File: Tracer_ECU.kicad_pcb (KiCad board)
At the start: 4 copper layers, 80 x 55 mm, 166 parts, among them IC1 R5F572TFADFP#30, IC2 MPU-6500, IC3 DRV8320HRTVR, IC4 DRV8320HRTVR, IC5 DRV8320HRTVR, J1 BAT, J10 ENC2, J11 SENS2, J13 SDC, J14 ENC3, J2 DBG, J3 SENS1, J4 MOT3, J5 MOT1, J6 LIGHIT, J8 MOT2, J9 ENC1, Q1 TJ60S04M3L, Q10 FDS6898A, Q11 FDS6898A, Q12 FDS6898A, Q2 FDS6898A, Q3 FDS6898A, Q4 FDS6898A, Q6 IRLML6344TRPBF, Q7 FDS6898A, Q8 FDS6898A, Q9 FDS6898A, SW1 SW_SPDT, SW2 SW_Push, SW4 SW_Push, SW5 SW_Push, U1 NJM2732, U2 AZ1117-3.3, Y1 CSTNE20M

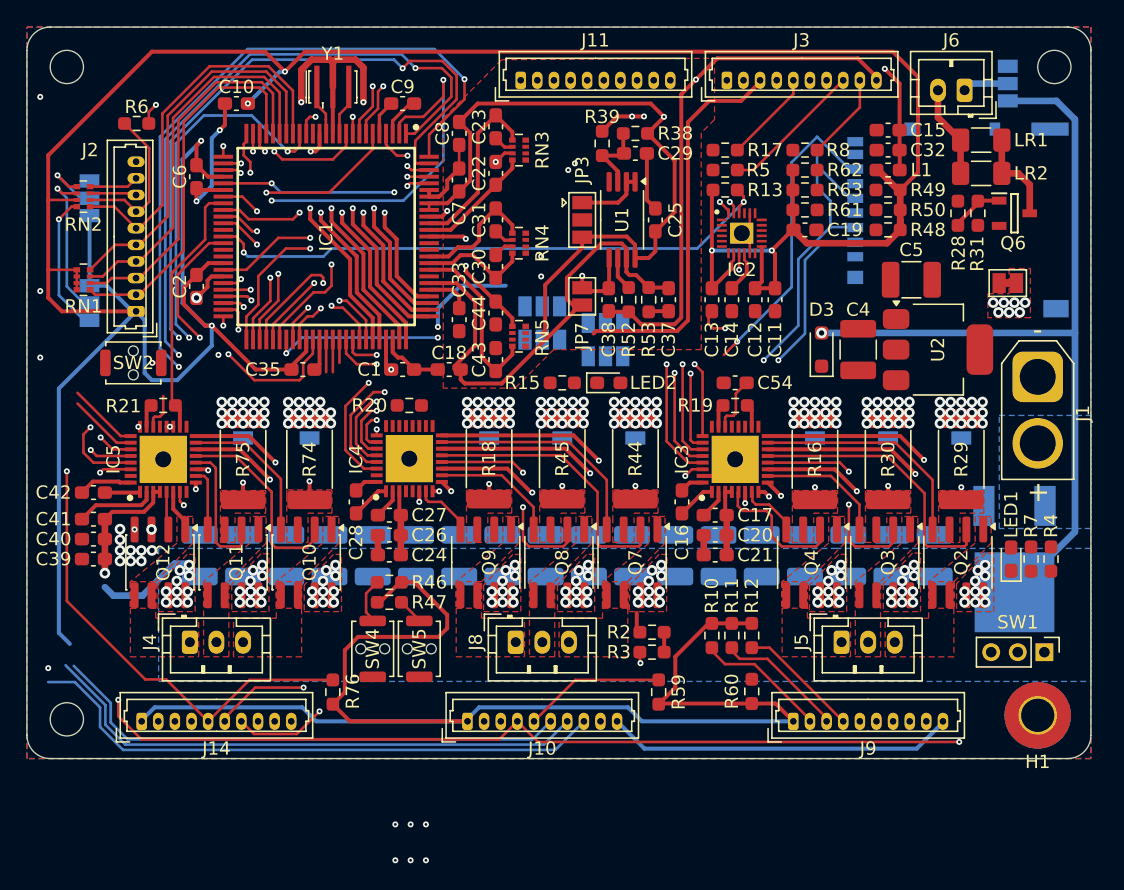
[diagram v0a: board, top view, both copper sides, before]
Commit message: PCB配線完了.(未配線ゼロ)
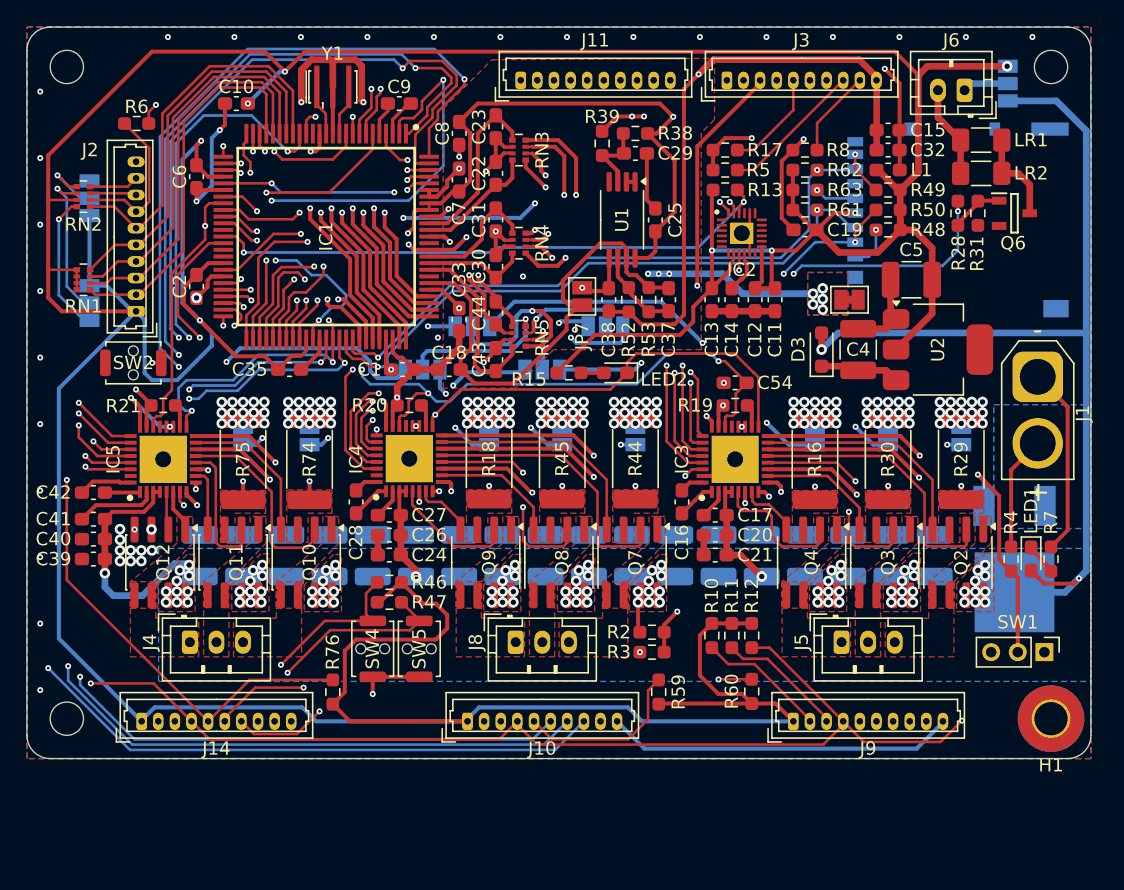
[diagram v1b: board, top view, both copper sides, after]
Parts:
- removed JP3: Jumper, Jumper:SolderJumper-3_P1.3mm_Open_Pad1.0x1.5mm
- moved JP5 12.0 mm to (150.3, 85.2), turned to 180 degrees
- moved JP4 10.2 mm to (122.0, 87.2)
- moved JP2 10.2 mm to (118.2, 90.5)
- moved R4 3.00 mm to (162.5, 104.8)
- moved JP9 2.25 mm to (127.2, 90.5)
- moved LED1 1.50 mm to (164.0, 104.8), turned to -90 degrees
- moved R7 1.50 mm to (165.5, 104.8)
- moved H1 1.03 mm to (165.5, 116.8)
- moved C35 1.00 mm to (108.2, 90.5)
- moved LED2 0.90 mm to (132.8, 90.8), turned to 180 degrees
- moved R15 0.90 mm to (129.2, 90.8)
- moved JP11 0.50 mm to (147.8, 95.5)
- moved JP12 0.50 mm to (123.2, 95.5)
- moved JP13 0.50 mm to (128.8, 95.5)
- moved JP14 0.50 mm to (134.2, 95.5)
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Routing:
- net AN201: track 4.86 -> 74.0 mm, vias 0 -> 4
- net PB2(GD_EN): track 24.2 -> 88.7 mm, vias 0 -> 4
- net P30: track 4.42 -> 64.4 mm, vias 0 -> 3
- net GNDA: track 88.0 -> 145.9 mm, vias 11 -> 17
- net P24: track 5.45 -> 62.9 mm, vias 0 -> 3
- net IRQ15: track 14.0 -> 65.3 mm, vias 1 -> 4
- net VCC: track 352.1 -> 399.6 mm, vias 7 -> 9
- net Mot.1_Ru+: track 6.04 -> 38.2 mm, vias 2 -> 3
- net Net-(JP10-A): track 0.00 -> 31.6 mm, vias 0 -> 2
- net Net-(JP16-A): track 19.1 -> 46.5 mm, vias 0 -> 2
- net Mot.3_SLB: track 7.76 -> 34.0 mm, vias 2 -> 3
- net Mot.1_Ru-: track 0.00 -> 25.5 mm, vias 19 -> 2
- net SMOSI12: track 21.9 -> 46.4 mm
- net Mot.1_SLB: track 34.2 -> 58.7 mm
- net PGAVSS1: track 3.05 -> 26.4 mm, vias 0 -> 4
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- added copper zone on B.Cu, net GNDA
- added copper zone on F.Cu, net Mot.1_SLB
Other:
- outline, holes or cut-outs redrawn

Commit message: バスバー用銅箔追加 レイアウト微調整
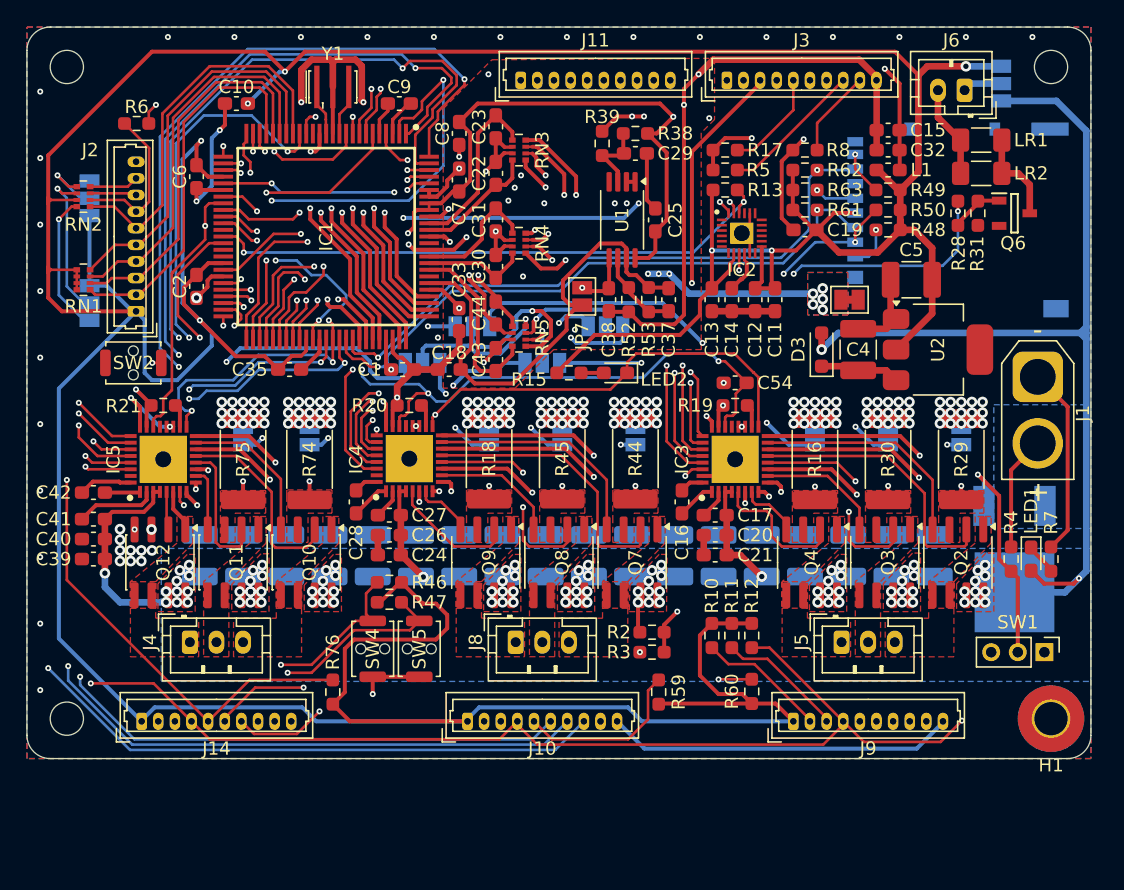
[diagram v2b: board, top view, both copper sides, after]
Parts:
- moved JP2 0.50 mm to (118.2, 90.0)
- moved JP8 0.50 mm to (161.8, 69.0)
- moved JP9 0.50 mm to (127.2, 90.0)
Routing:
- net Mot.1_SLB: track 58.7 -> 57.9 mm
- net Net-(JP15-A): track 44.8 -> 44.0 mm
- net Mot.3_SLB: track 34.0 -> 34.7 mm
- net GNDA: track 145.9 -> 145.3 mm, vias 17 -> 26
- net AN216/IRQ7: track 55.2 -> 55.9 mm
- net VCC: track 399.6 -> 400.2 mm
- net Net-(JP9-C): track 4.65 -> 4.11 mm
- net Mot.1_Ru+: track 38.2 -> 38.7 mm
- net +12V: track 111.0 -> 110.5 mm
- net Net-(J6-Pin_1): track 3.46 -> 2.96 mm

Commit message: LCD用ポートコネクタを追加．(I2C端子)
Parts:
- added J7: LCD, Connector_Molex:Molex_PicoBlade_53047-0510_1x05_P1.25mm_Vertical, F.Cu at (95.8, 68.8)
- moved C10 0.50 mm to (104.8, 70.5)
- moved C2 0.50 mm to (101.2, 84.8)
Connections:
- IC1 pad 40: unconnected-(IC1-PA1-Pad40) -> SSCL11
- IC1 pad 41: unconnected-(IC1-PA0-Pad41) -> SSDA11
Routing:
- net SSDA11: track 0.00 -> 25.6 mm, vias 0 -> 1
- net SSCL11: track 0.00 -> 23.6 mm, vias 0 -> 1
- net Mot.3_SLA: track 128.2 -> 120.5 mm
- net VCC: track 400.2 -> 393.9 mm
- net RES#: track 19.8 -> 23.0 mm, vias 2 -> 1
- net SSLA3: track 82.3 -> 84.3 mm
- net MTCLKD: track 112.3 -> 114.3 mm
- net MTCLKC: track 111.4 -> 113.4 mm
- net IRQ4: track 116.5 -> 118.4 mm
- net PB2(GD_EN): track 88.7 -> 90.2 mm
- net RSPCKA: track 180.4 -> 179.0 mm
- net SSLA1: track 83.2 -> 84.4 mm
- net GTIOC0A: track 41.5 -> 40.3 mm
- net MISOA: track 172.2 -> 171.2 mm
- net MOSIA: track 178.0 -> 177.0 mm
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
